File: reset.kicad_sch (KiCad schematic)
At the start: 22 parts, among them J4 MAINCLK

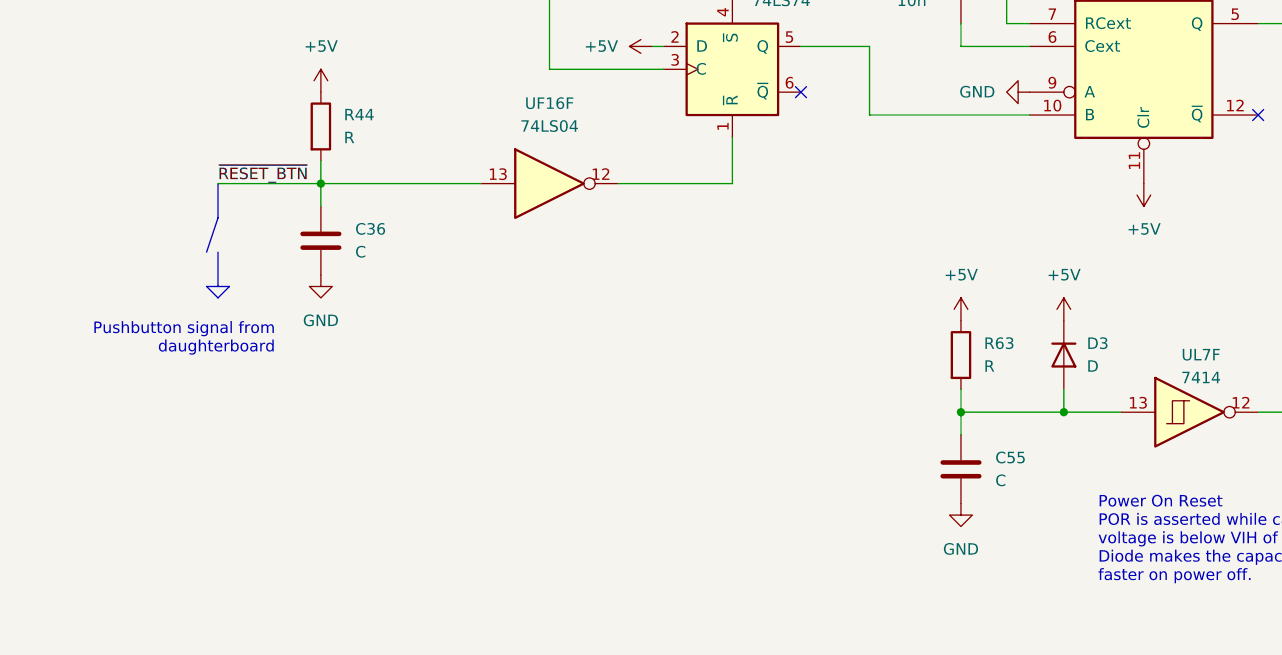
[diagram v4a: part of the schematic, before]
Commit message: pcb: added all the connector, 99% routed
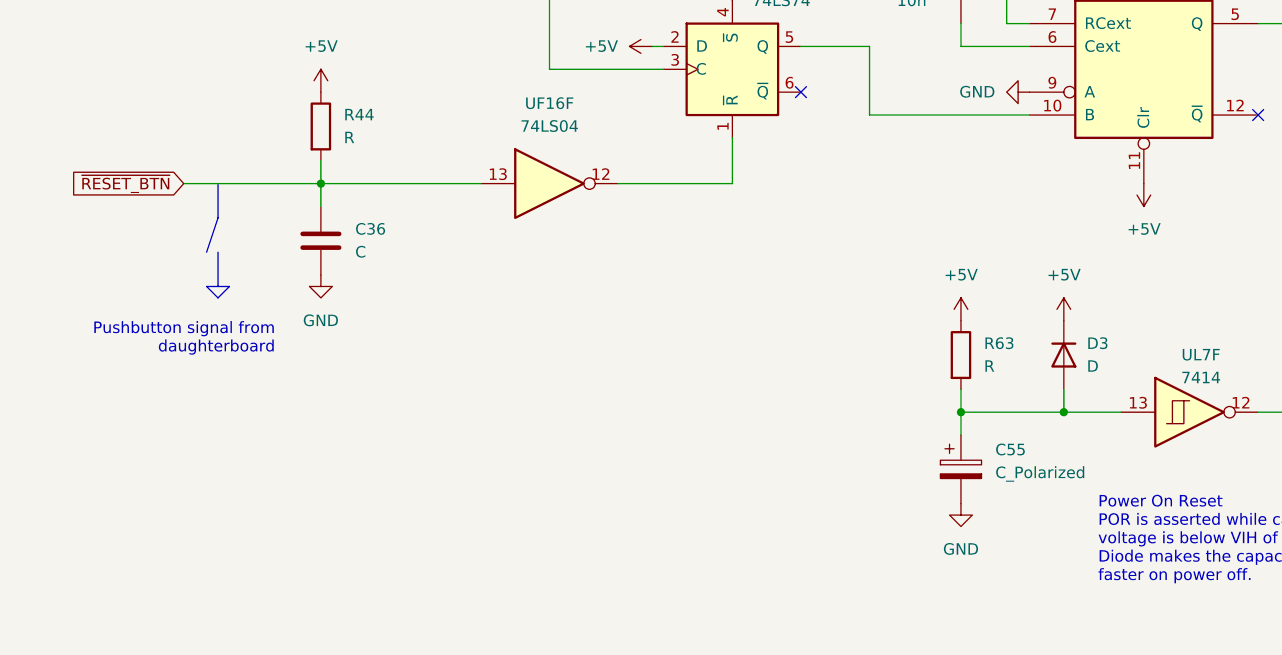
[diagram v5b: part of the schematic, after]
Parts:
- removed C55: C, Capacitor_THT:C_Disc_D4.3mm_W1.9mm_P5.00mm, symbol Device:C
- added C55: C_Polarized, Capacitor_THT:CP_Radial_D5.0mm_P2.50mm, symbol Device:C_Polarized
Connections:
- net GND: now also C55.2
- net at D3.2 (A), R63.2, UL7.13: now also C55.1
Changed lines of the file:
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@@
 	(wire
 		(pts
-			(xy 29.21 72.39) (xy 40.64 72.39)
+			(xy 25.4 72.39) (xy 40.64 72.39)
 		)
 		(stroke
@@
 		)
 	)
-	(label "~{RESET_BTN}"
-		(at 29.21 72.39 0)
-		(effects
-			(font
-				(size 1.27 1.27)
-			)
-			(justify left bottom)
-		)
-	)
 	(label "POR"
 		(at 147.32 97.79 0)
@@
 		)
 	)
+	(global_label "~{RESET_BTN}"
+		(shape input)
+		(at 25.4 72.39 180)
+		(fields_autoplaced yes)
+		(effects
+			(font
+				(size 1.27 1.27)
+			)
+			(justify right)
+		)
+		(property "Intersheetrefs" "${INTERSHEET_REFS}"
+			(at 12.134 72.39 0)
+			(effects
+				(font
+					(size 1.27 1.27)
+				)
+				(justify right)
+				(hide yes)
+			)
+		)
+	)
 	(global_label "RESET"
 		(shape output)
@@
 	)
 	(symbol
+		(lib_id "Device:C_Polarized")
+		(at 111.76 104.14 0)
+		(unit 1)
+		(exclude_from_sim no)
+		(in_bom yes)
+		(on_board yes)
+		(dnp no)
+		(fields_autoplaced yes)
+		(property "Reference" "C55"
+			(at 115.57 101.9809 0)
+			(effects
+				(font
+					(size 1.27 1.27)
+				)
+				(justify left)
+			)
+		)
+		(property "Value" "C_Polarized"
+			(at 115.57 104.5209 0)
+			(effects
+				(font
+					(size 1.27 1.27)
+				)
+				(justify left)
+			)
+		)
+		(property "Footprint" "Capacitor_THT:CP_Radial_D5.0mm_P2.50mm"
+			(at 112.7252 107.95 0)
+			(effects
+				(font
+					(size 1.27 1.27)
+				)
+				(hide yes)
+			)
+		)
+		(property "Datasheet" "~"
+			(at 111.76 104.14 0)
+			(effects
+				(font
+					(size 1.27 1.27)
+				)
+				(hide yes)
+			)
+		)
+		(property "Description" "Polarized capacitor"
+			(at 111.76 104.14 0)
+			(effects
+				(font
+					(size 1.27 1.27)
+				)
+				(hide yes)
+			)
+		)
+		(pin "2"
+		)
+		(pin "1"
+		)
+		(instances
+			(project ""
+				(path "/12a6dbe3-008d-4c5b-88f6-9f1c816060be/d9e42cc5-3ed8-41e5-aab1-e3ef5c13a809"
+					(reference "C55")
+					(unit 1)
+				)
+			)
+		)
+	)
+	(symbol
 		(lib_id "power:+5V")
 		(at 20.32 144.78 0)
@@
 				)
 			)
-		)
-	)
-	(symbol
-		(lib_id "Device:C")
-		(at 111.76 104.14 0)
-		(unit 1)
-		(exclude_from_sim no)
-		(in_bom yes)
-		(on_board yes)
-		(dnp no)
-		(fields_autoplaced yes)
-		(property "Reference" "C55"
-			(at 115.57 102.87 0)
-			(effects
-				(font
-					(size 1.27 1.27)
-				)
-				(justify left)
-			)
-		)
-		(property "Value" "C"
-			(at 115.57 105.41 0)
-			(effects
-				(font
-					(size 1.27 1.27)
-				)
-				(justify left)
-			)
-		)
-		(property "Footprint" "Capacitor_THT:C_Disc_D4.3mm_W1.9mm_P5.00mm"
-			(at 112.7252 107.95 0)
-			(effects
-				(font
-					(size 1.27 1.27)
-				)
-				(hide yes)
-			)
-		)
-		(property "Datasheet" "~"
-			(at 111.76 104.14 0)
-			(effects
-				(font
-					(size 1.27 1.27)
-				)
-				(hide yes)
-			)
-		)
-		(property "Description" ""
-			(at 111.76 104.14 0)
-			(effects
-				(font
-					(size 1.27 1.27)
-				)
-			)
-		)
-		(pin "1"
-		)
-		(pin "2"
-		)
-		(instances
-			(project "ceda"
-				(path "/12a6dbe3-008d-4c5b-88f6-9f1c816060be/d9e42cc5-3ed8-41e5-aab1-e3ef5c13a809"
-					(reference "C55")
-					(unit 1)
-				)
-			)

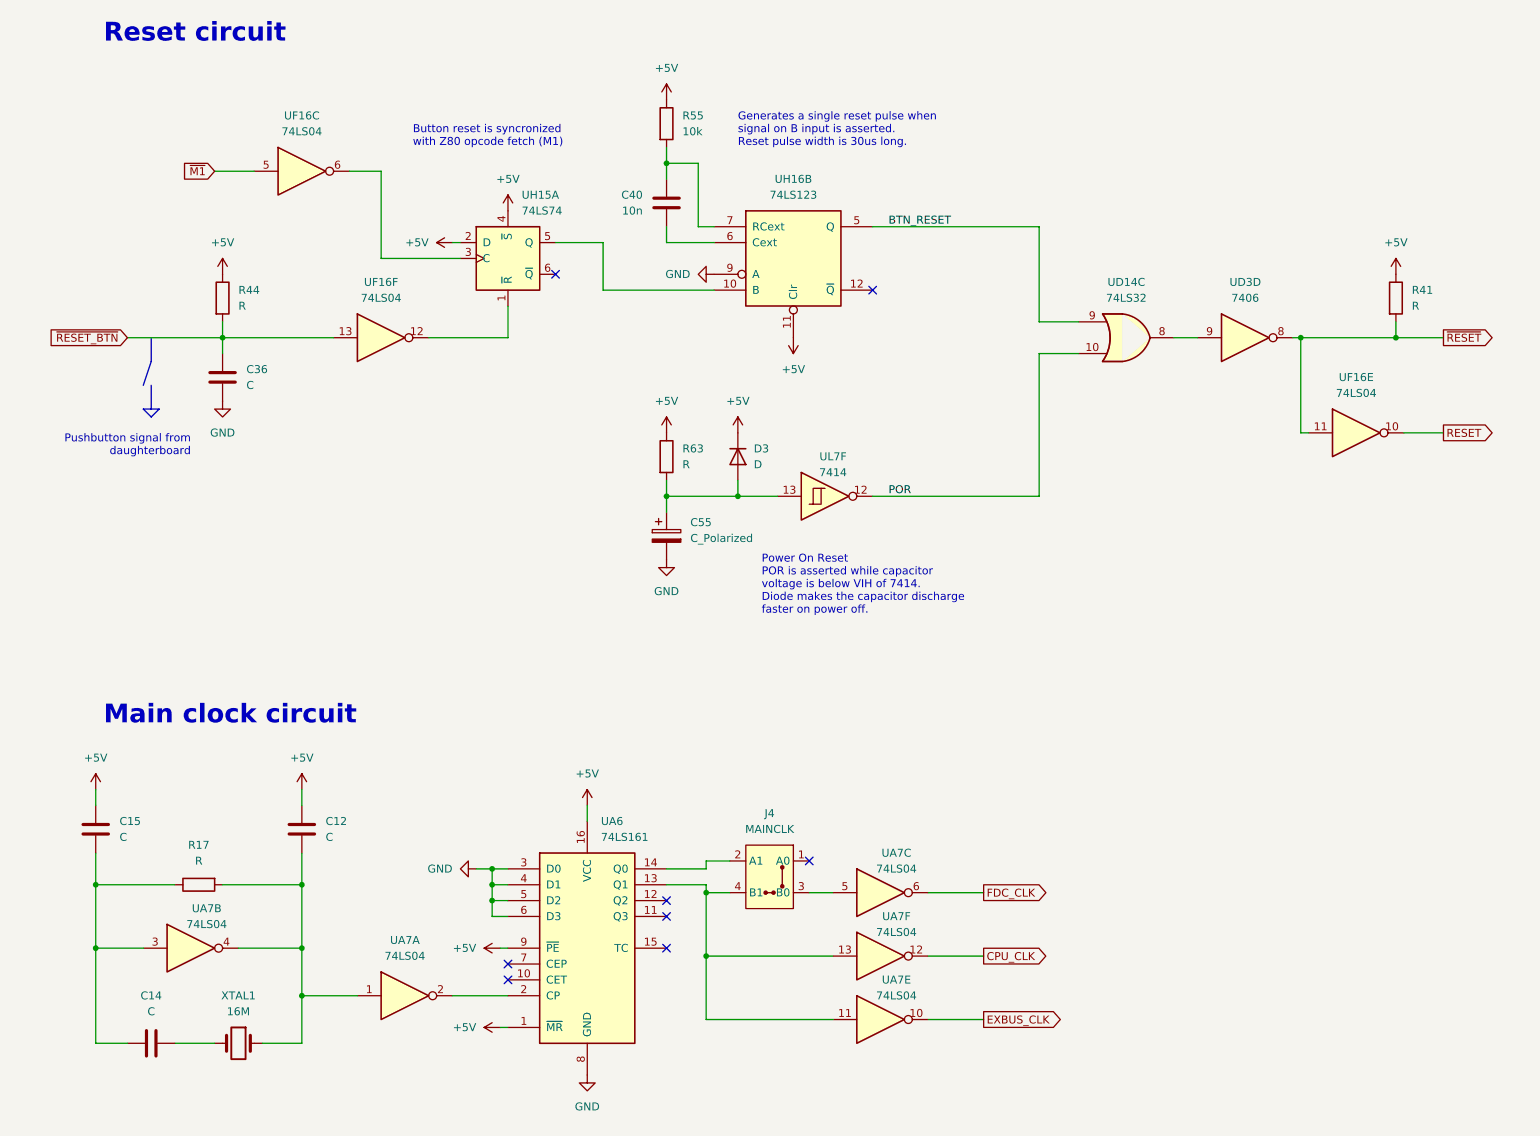
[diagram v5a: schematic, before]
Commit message: pcb and sch: finished routing and fixing connections
There are still some minor inconsistencies (/WR, /RD, one PRINTER
signal), some passives missing (decoupling caps, power stage), but the
schematic and the pcb should be more or less complete.
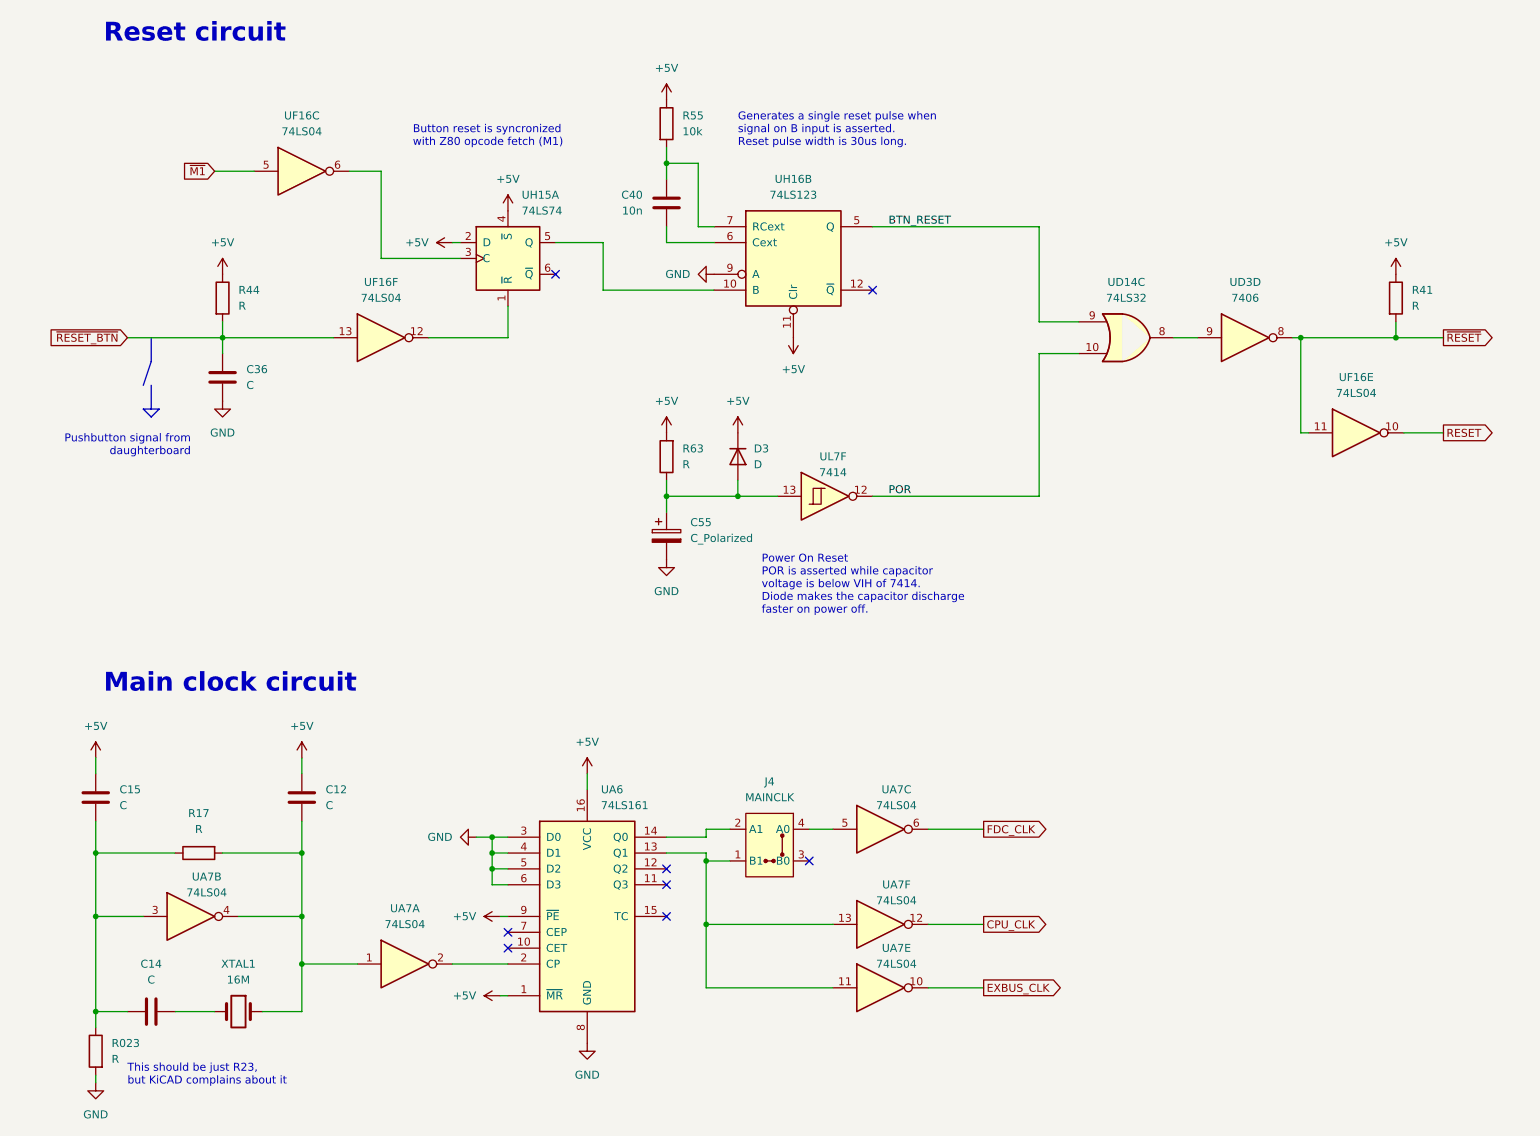
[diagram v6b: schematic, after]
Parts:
- added R023: R, Resistor_THT:R_Axial_DIN0204_L3.6mm_D1.6mm_P5.08mm_Vertical, symbol Device:R
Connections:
- net +5V: now also R63.2; no longer R63.1
- net GND: now also R023.2
- net at C55.1, D3.2 (A), UL7.13: now also R63.1; no longer R63.2
- net at UA6.13 (Q1), UA7.11, UA7.13: now also J4.1 (B1); no longer J4.4 (B1)
- net at C14.2, C15.1, R17.1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: now also R023.1
- net at UA7.5: now also J4.4 (A0); no longer J4.3 (B0)
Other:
- note added: "This should be just R23, but KiCAD complains about it"
- moved on the sheet: C12, C14, C15, J4, R17, R63, UA6, UA7A, UA7B, UA7C, UA7E, UA7F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

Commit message: pcb: proper symbols for MAP and MAINCLK
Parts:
- J4: footprint Connector_PinHeader_2.54mm:PinHeader_2x02_P2.54mm_Vertical -> Ceda:MAINCLK
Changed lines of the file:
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@@
 			)
 		)
-		(property "Footprint" "Connector_PinHeader_2.54mm:PinHeader_2x02_P2.54mm_Vertical"
+		(property "Footprint" "Ceda:MAINCLK"
 			(at 128.27 156.21 0)
 			(effects
